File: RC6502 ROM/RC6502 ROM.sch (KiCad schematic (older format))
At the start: 13 parts, among them J1 CONN_01X39, U1 28C256, U2 74HCT00, U3 74HCT00

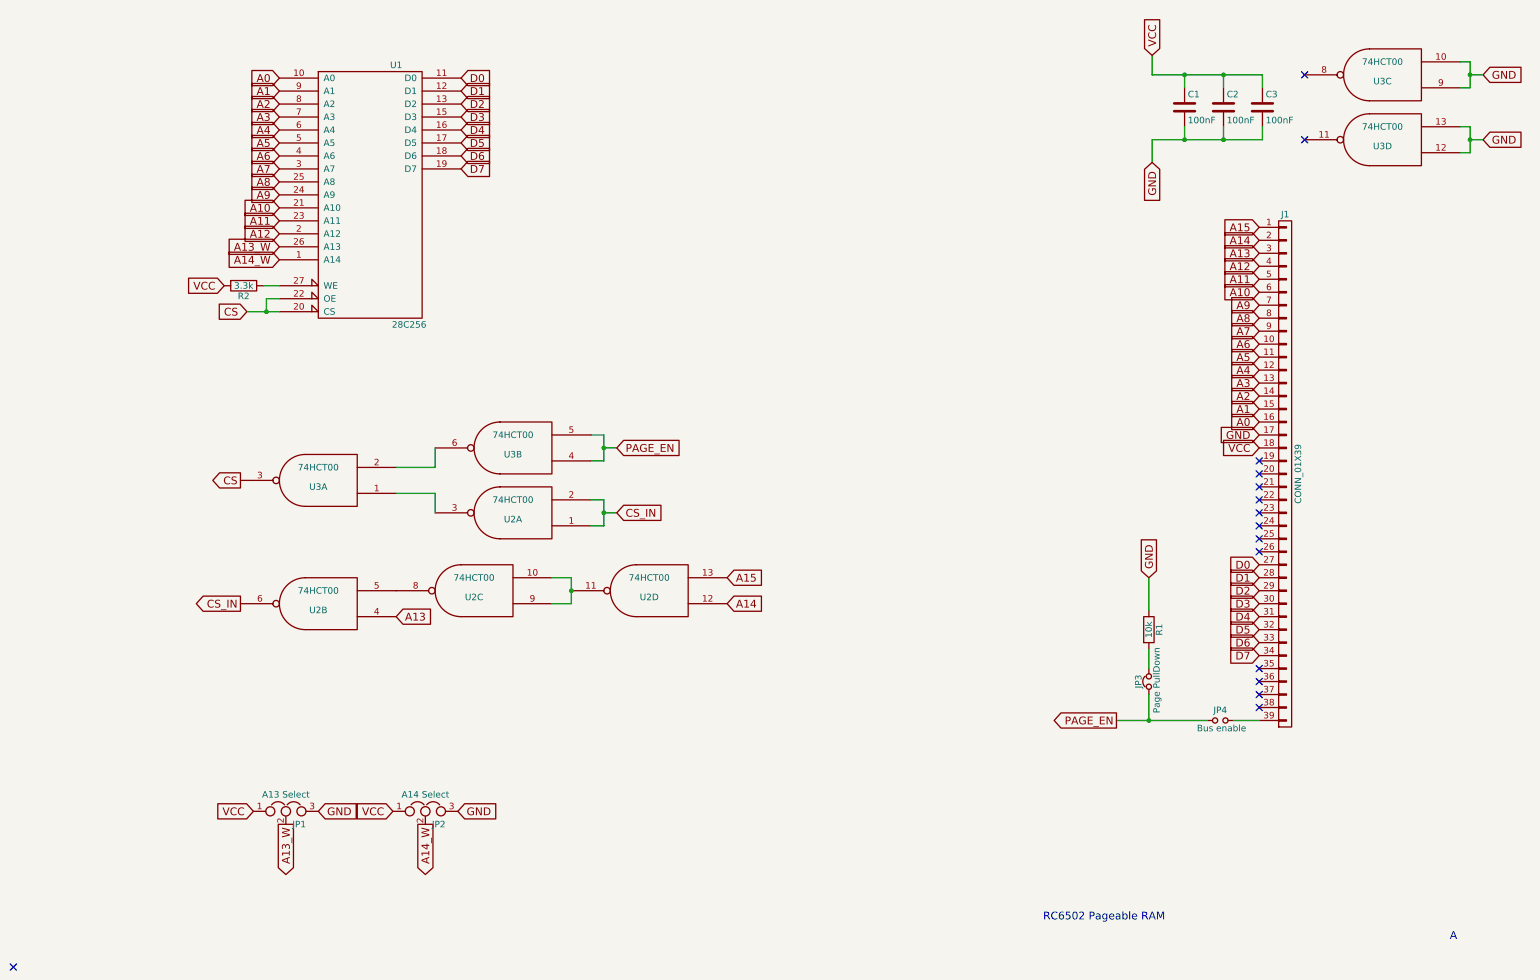
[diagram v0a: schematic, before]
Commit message: Added jumper select to decide if paging hardware installed
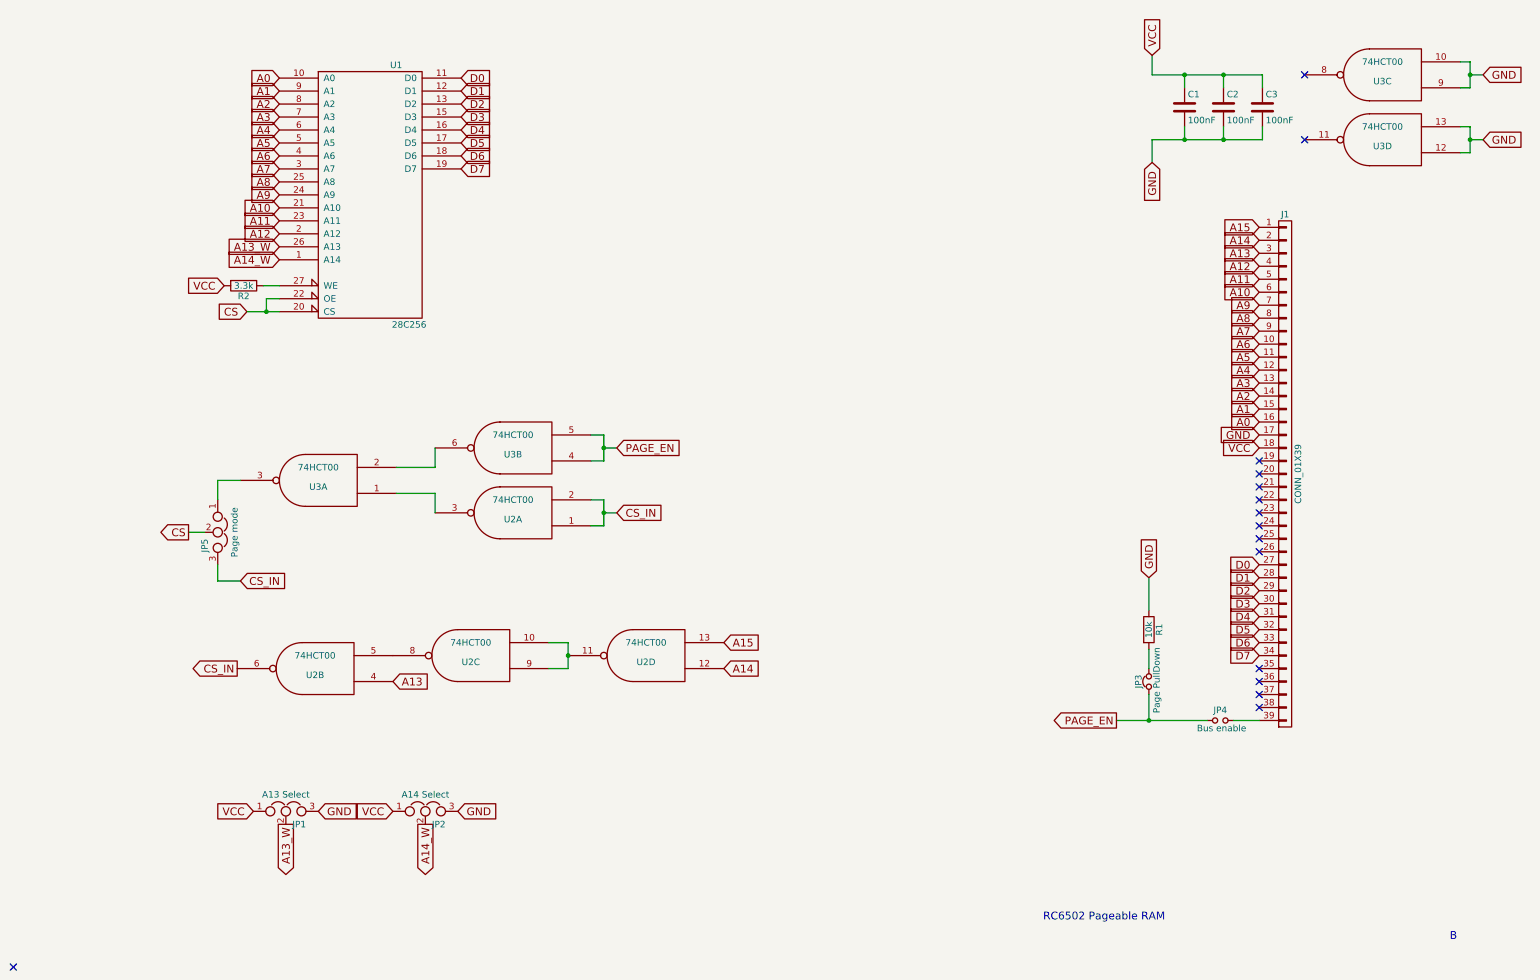
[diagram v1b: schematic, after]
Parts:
- added JP5: Page mode, Pin_Headers:Pin_Header_Angled_1x03_Pitch2.54mm, symbol Jumper_NC_Dual
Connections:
- net CS: now also JP5.2; no longer U3.3
- net CS_IN: now also JP5.3
- new net: JP5.1, U3.3
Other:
- note added: "B"
- note removed: "A"
- moved on the sheet: U2B, U2C, U2D
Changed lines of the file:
@@
 RC6502 Pageable RAM
 Text Notes 10625 7650 2    60   ~ 0
-A
+B
 NoConn ~ -500 7850
 $Comp
@@
 L 74HCT00 U2
 U 4 1 590F02B0
-P 4400 4950
-F 0 "U2" H 4400 5000 50  0000 C CNN
-F 1 "74HCT00" H 4400 4850 50  0000 C CNN
-F 2 "Housings_DIP:DIP-14_W7.62mm_Socket" H 4400 4950 50  0001 C CNN
-F 3 "" H 4400 4950 50  0001 C CNN
-	4    4400 4950
+P 4375 5450
+F 0 "U2" H 4375 5500 50  0000 C CNN
+F 1 "74HCT00" H 4375 5350 50  0000 C CNN
+F 2 "Housings_DIP:DIP-14_W7.62mm_Socket" H 4375 5450 50  0001 C CNN
+F 3 "" H 4375 5450 50  0001 C CNN
+	4    4375 5450
 	-1   0    0    1
 $EndComp
@@
 L 74HCT00 U2
 U 3 1 590F036D
-P 3050 4950
-F 0 "U2" H 3050 5000 50  0000 C CNN
-F 1 "74HCT00" H 3050 4850 50  0000 C CNN
-F 2 "Housings_DIP:DIP-14_W7.62mm_Socket" H 3050 4950 50  0001 C CNN
-F 3 "" H 3050 4950 50  0001 C CNN
-	3    3050 4950
+P 3025 5450
+F 0 "U2" H 3025 5500 50  0000 C CNN
+F 1 "74HCT00" H 3025 5350 50  0000 C CNN
+F 2 "Housings_DIP:DIP-14_W7.62mm_Socket" H 3025 5450 50  0001 C CNN
+F 3 "" H 3025 5450 50  0001 C CNN
+	3    3025 5450
 	-1   0    0    1
 $EndComp
@@
 L 74HCT00 U2
 U 2 1 590F04E0
-P 1850 5050
-F 0 "U2" H 1850 5100 50  0000 C CNN
-F 1 "74HCT00" H 1850 4950 50  0000 C CNN
-F 2 "Housings_DIP:DIP-14_W7.62mm_Socket" H 1850 5050 50  0001 C CNN
-F 3 "" H 1850 5050 50  0001 C CNN
-	2    1850 5050
-	-1   0    0    1
-$EndComp
-Text GLabel 5000 4850 2    60   Input ~ 0
+P 1825 5550
+F 0 "U2" H 1825 5600 50  0000 C CNN
+F 1 "74HCT00" H 1825 5450 50  0000 C CNN
+F 2 "Housings_DIP:DIP-14_W7.62mm_Socket" H 1825 5550 50  0001 C CNN
+F 3 "" H 1825 5550 50  0001 C CNN
+	2    1825 5550
+	-1   0    0    1
+$EndComp
+Text GLabel 4975 5350 2    60   Input ~ 0
 A15
-Text GLabel 5000 5050 2    60   Input ~ 0
+Text GLabel 4975 5550 2    60   Input ~ 0
 A14
-Text GLabel 2450 5150 2    60   Input ~ 0
+Text GLabel 2425 5650 2    60   Input ~ 0
 A13
 Text GLabel 1300 2800 0    60   Input ~ 0
 CS
-Text GLabel 1250 5050 0    60   Output ~ 0
+Text GLabel 1225 5550 0    60   Output ~ 0
 CS_IN
 $Comp
@@
 	8250 5100 8250 4850
 Wire Wire Line
-	3800 4850 3650 4850
-Connection ~ 3800 4950
-Wire Wire Line
-	3800 4850 3800 5050
-Wire Wire Line
-	3800 5050 3650 5050
+	3775 5350 3625 5350
+Connection ~ 3775 5450
+Wire Wire Line
+	3775 5350 3775 5550
+Wire Wire Line
+	3775 5550 3625 5550
 Text GLabel 4150 3850 2    60   Input ~ 0
 PAGE_EN
 Text GLabel 4150 4350 2    60   Input ~ 0
 CS_IN
-Text GLabel 1250 4100 0    60   Output ~ 0
+Text GLabel 850  4500 0    60   Output ~ 0
 CS
 $Comp
@@
 	3950 3750 4050 3750
 Connection ~ 4050 3850
-Wire Wire Line
-	2750 4350 2750 4200
 Wire Wire Line
 	2750 4200 2450 4200
@@
 Wire Wire Line
 	1425 2600 1550 2600
+$Comp
+L Jumper_NC_Dual JP5
+U 1 1 592A3680
+P 1075 4500
+F 0 "JP5" H 1125 4400 50  0000 L CNN
+F 1 "Page mode" H 1075 4600 50  0000 C BNN
+F 2 "Pin_Headers:Pin_Header_Angled_1x03_Pitch2.54mm" H 1075 4500 50  0001 C CNN
+F 3 "" H 1075 4500 50  0001 C CNN
+	1    1075 4500
+	0    1    1    0
+$EndComp
+Wire Wire Line
+	850  4500 975  4500
+Wire Wire Line
+	1075 4250 1075 4100
+Wire Wire Line
+	1075 4100 1250 4100
+Wire Wire Line
+	1075 4875 1075 4750
+Wire Wire Line
+	2750 4200 2750 4350
+Wire Wire Line
+	1075 4875 1250 4875
+Text GLabel 1250 4875 2    60   Input ~ 0
+CS_IN
 $EndSCHEMATC

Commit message: ROM revision B
JP5 inside U3 footprint is used to designate wether paging hardware is installed or not (skip  C3 and U3).
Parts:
- JP5: footprint Pin_Headers:Pin_Header_Angled_1x03_Pitch2.54mm -> Pin_Headers:Pin_Header_Straight_1x03_Pitch2.54mm
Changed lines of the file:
@@
 F 0 "JP5" H 1125 4400 50  0000 L CNN
 F 1 "Page mode" H 1075 4600 50  0000 C BNN
-F 2 "Pin_Headers:Pin_Header_Angled_1x03_Pitch2.54mm" H 1075 4500 50  0001 C CNN
+F 2 "Pin_Headers:Pin_Header_Straight_1x03_Pitch2.54mm" H 1075 4500 50  0001 C CNN
 F 3 "" H 1075 4500 50  0001 C CNN
 	1    1075 4500
